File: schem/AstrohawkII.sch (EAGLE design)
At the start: 3 parts, among them J1 RASPBERRYPI-40-PIN-GPIO_PTH_N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

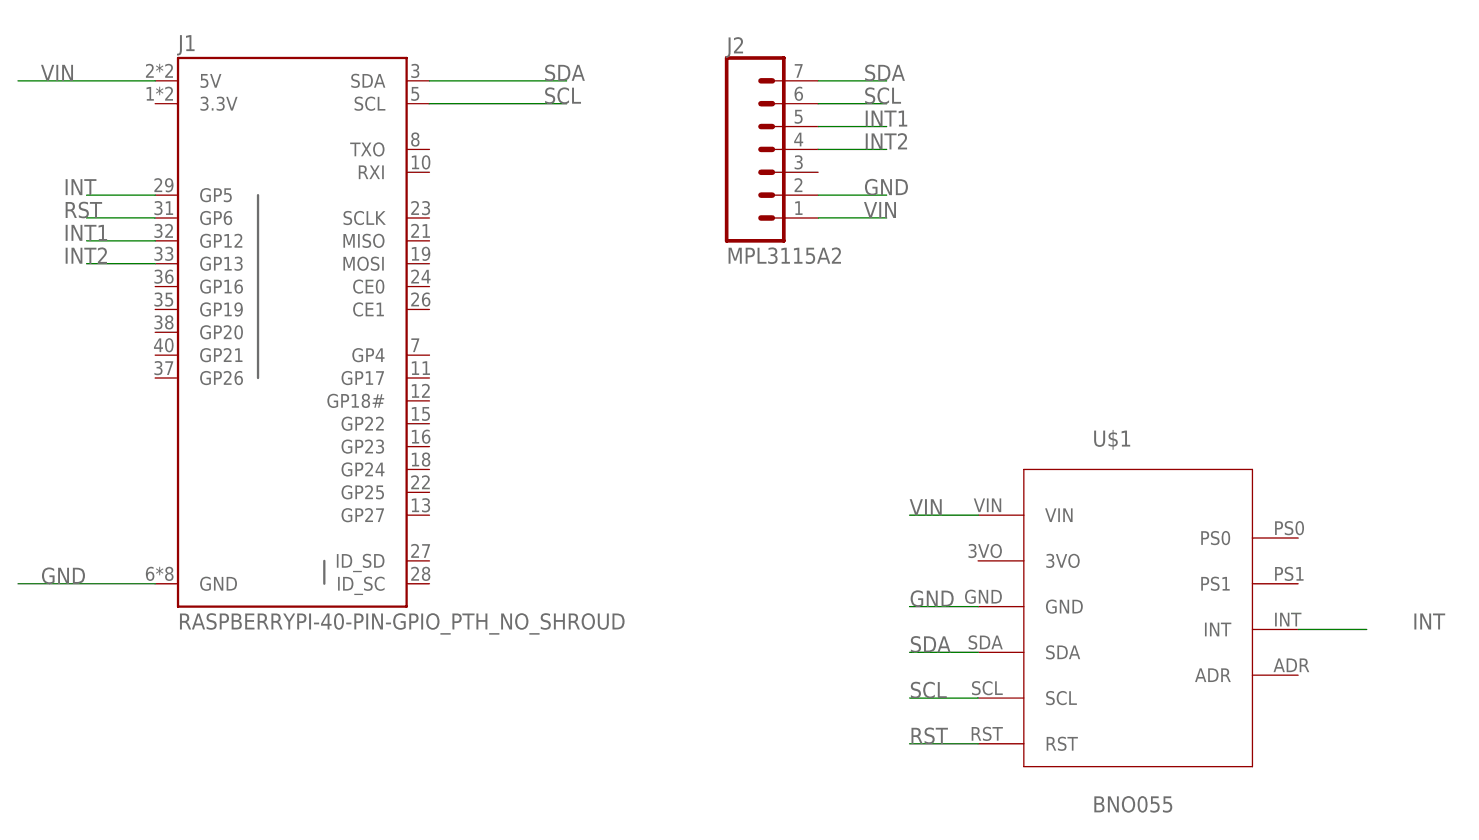
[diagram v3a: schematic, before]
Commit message: adds finishing touches to pcb design
1. Altimeter device (package/symbol) added with drill holes for screws
2. Drill holes and silk screen updated for IMU device
3. Hole cutout added to account for the camera cable
4. Copper re-routed for Altimeter
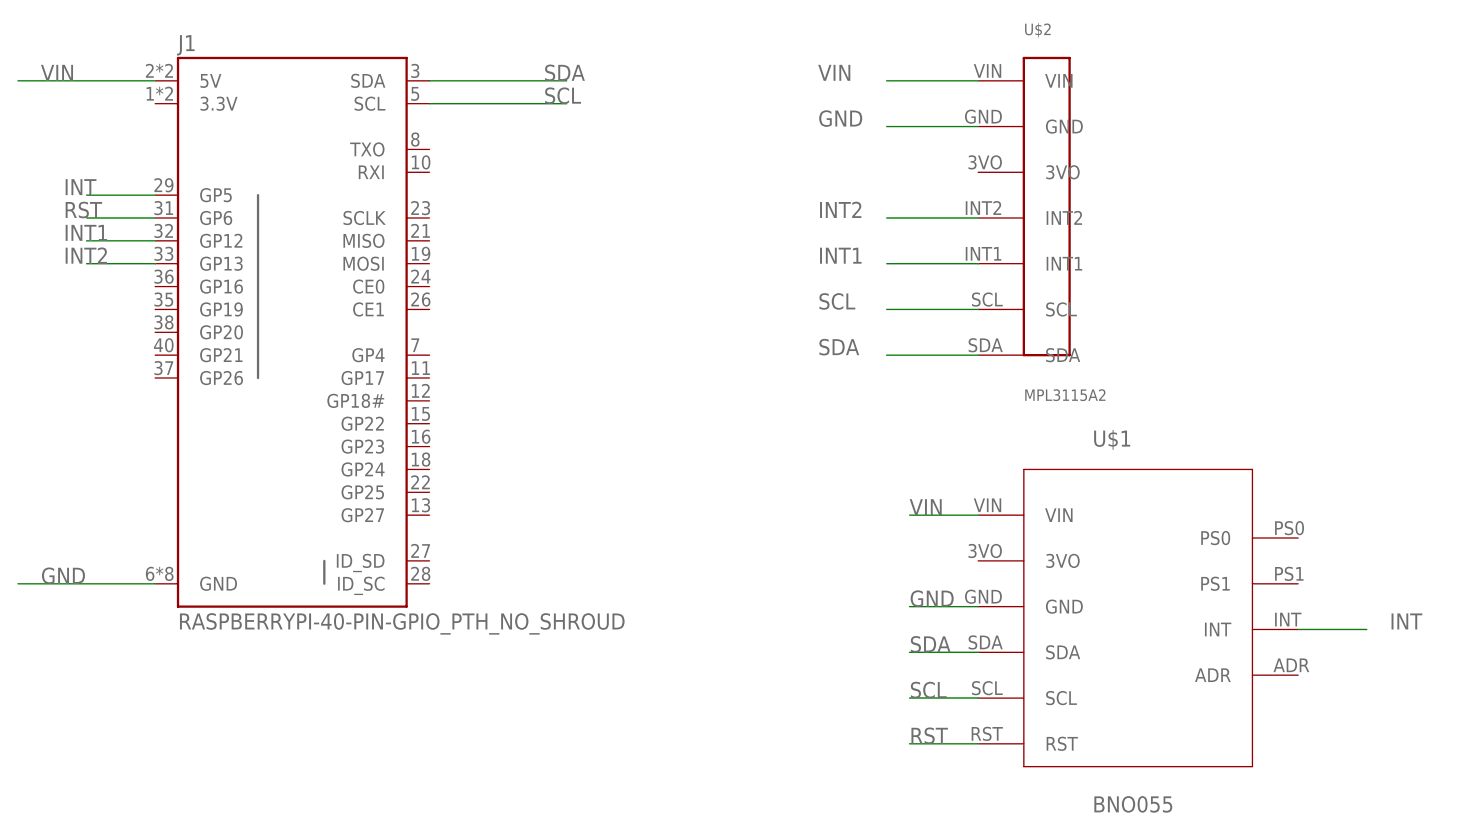
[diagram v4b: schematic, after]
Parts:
- removed J2: (no value), SparkFun-Connectors:CONN_07
- added U$2: MPL3115A2, rocketry:MPL3115A2
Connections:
- net GND: now also U$2.GND; no longer J2.2
- net INT1: now also U$2.INT1; no longer J2.5
- net INT2: now also U$2.INT2; no longer J2.4
- net SCL: now also U$2.SCL; no longer J2.6
- net SDA: now also U$2.SDA; no longer J2.7
- net VIN: now also U$2.VIN; no longer J2.1
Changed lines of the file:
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@@
 <parts>
 <part name="J1" library="SparkFun-Connectors" deviceset="RASPBERRYPI-40-PIN-GPIO" device="_PTH_NO_SHROUD"/>
-<part name="J2" library="SparkFun-Connectors" deviceset="CONN_07" device="">
-<attribute name="MPL3115A2" value=""/>
-</part>
 <part name="U$1" library="rocketry" deviceset="BNO055" device=""/>
+<part name="U$2" library="rocketry" deviceset="MPL3115A2" device=""/>
 </parts>
 <sheets>
@@
 <attribute name="VALUE" x="12.7" y="38.1" size="1.778" layer="96"/>
 </instance>
-<instance part="J2" gate="J1" x="78.74" y="88.9" smashed="yes">
-<attribute name="VALUE" x="73.66" y="78.994" size="1.778" layer="96" font="vector"/>
-<attribute name="NAME" x="73.66" y="102.108" size="1.778" layer="95" font="vector"/>
-<attribute name="MPL3115A2" x="73.66" y="78.74" size="1.778" layer="96" display="name"/>
-</instance>
 <instance part="U$1" gate="G$1" x="116.84" y="35.56"/>
+<instance part="U$2" gate="G$1" x="109.22" y="83.82"/>
 </instances>
 <busses>
@@
 <segment>
 <wire x1="137.16" y1="38.1" x2="144.78" y2="38.1" width="0.1524" layer="91"/>
-<label x="149.86" y="38.1" size="1.778" layer="95"/>
+<label x="147.32" y="38.1" size="1.778" layer="95"/>
 <pinref part="U$1" gate="G$1" pin="INT"/>
 </segment>
@@
 <net name="VIN" class="0">
 <segment>
-<pinref part="J2" gate="J1" pin="1"/>
-<wire x1="83.82" y1="83.82" x2="91.44" y2="83.82" width="0.1524" layer="91"/>
-<label x="88.9" y="83.82" size="1.778" layer="95"/>
+<wire x1="91.44" y1="99.06" x2="101.6" y2="99.06" width="0.1524" layer="91"/>
+<label x="83.82" y="99.06" size="1.778" layer="95"/>
+<pinref part="U$2" gate="G$1" pin="VIN"/>
 </segment>
 <segment>
@@
 <net name="GND" class="0">
 <segment>
-<pinref part="J2" gate="J1" pin="2"/>
-<wire x1="83.82" y1="86.36" x2="91.44" y2="86.36" width="0.1524" layer="91"/>
-<label x="88.9" y="86.36" size="1.778" layer="95"/>
+<wire x1="91.44" y1="93.98" x2="101.6" y2="93.98" width="0.1524" layer="91"/>
+<label x="83.82" y="93.98" size="1.778" layer="95"/>
+<pinref part="U$2" gate="G$1" pin="GND"/>
 </segment>
 <segment>
@@
 <net name="INT2" class="0">
 <segment>
-<pinref part="J2" gate="J1" pin="4"/>
-<wire x1="83.82" y1="91.44" x2="91.44" y2="91.44" width="0.1524" layer="91"/>
-<label x="88.9" y="91.44" size="1.778" layer="95"/>
+<wire x1="91.44" y1="83.82" x2="101.6" y2="83.82" width="0.1524" layer="91"/>
+<label x="83.82" y="83.82" size="1.778" layer="95"/>
+<pinref part="U$2" gate="G$1" pin="INT2"/>
 </segment>
 <segment>
@@
 <net name="INT1" class="0">
 <segment>
-<pinref part="J2" gate="J1" pin="5"/>
-<wire x1="83.82" y1="93.98" x2="91.44" y2="93.98" width="0.1524" layer="91"/>
-<label x="88.9" y="93.98" size="1.778" layer="95"/>
+<wire x1="91.44" y1="78.74" x2="101.6" y2="78.74" width="0.1524" layer="91"/>
+<label x="83.82" y="78.74" size="1.778" layer="95"/>
+<pinref part="U$2" gate="G$1" pin="INT1"/>
 </segment>
 <segment>
@@
 <net name="SCL" class="0">
 <segment>
-<pinref part="J2" gate="J1" pin="6"/>
-<wire x1="83.82" y1="96.52" x2="91.44" y2="96.52" width="0.1524" layer="91"/>
-<label x="88.9" y="96.52" size="1.778" layer="95"/>
+<wire x1="91.44" y1="73.66" x2="101.6" y2="73.66" width="0.1524" layer="91"/>
+<label x="83.82" y="73.66" size="1.778" layer="95"/>
+<pinref part="U$2" gate="G$1" pin="SCL"/>
 </segment>
 <segment>
@@
 <net name="SDA" class="0">
 <segment>
-<pinref part="J2" gate="J1" pin="7"/>
-<wire x1="83.82" y1="99.06" x2="91.44" y2="99.06" width="0.1524" layer="91"/>
-<label x="88.9" y="99.06" size="1.778" layer="95"/>
+<wire x1="91.44" y1="68.58" x2="101.6" y2="68.58" width="0.1524" layer="91"/>
+<label x="83.82" y="68.58" size="1.778" layer="95"/>
+<pinref part="U$2" gate="G$1" pin="SDA"/>
 </segment>
 <segment>
